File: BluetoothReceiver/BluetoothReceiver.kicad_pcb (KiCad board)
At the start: 4 copper layers, 48.4 x 40 mm, 54 parts, among them J1 EXT_ANTENNA, J2 SWD, J3 SPKR/HP, J4 MIC, J5 I2S, J6 I2C/UART, J7 USB, J8 3.3V, U1 STM32F413CHUx

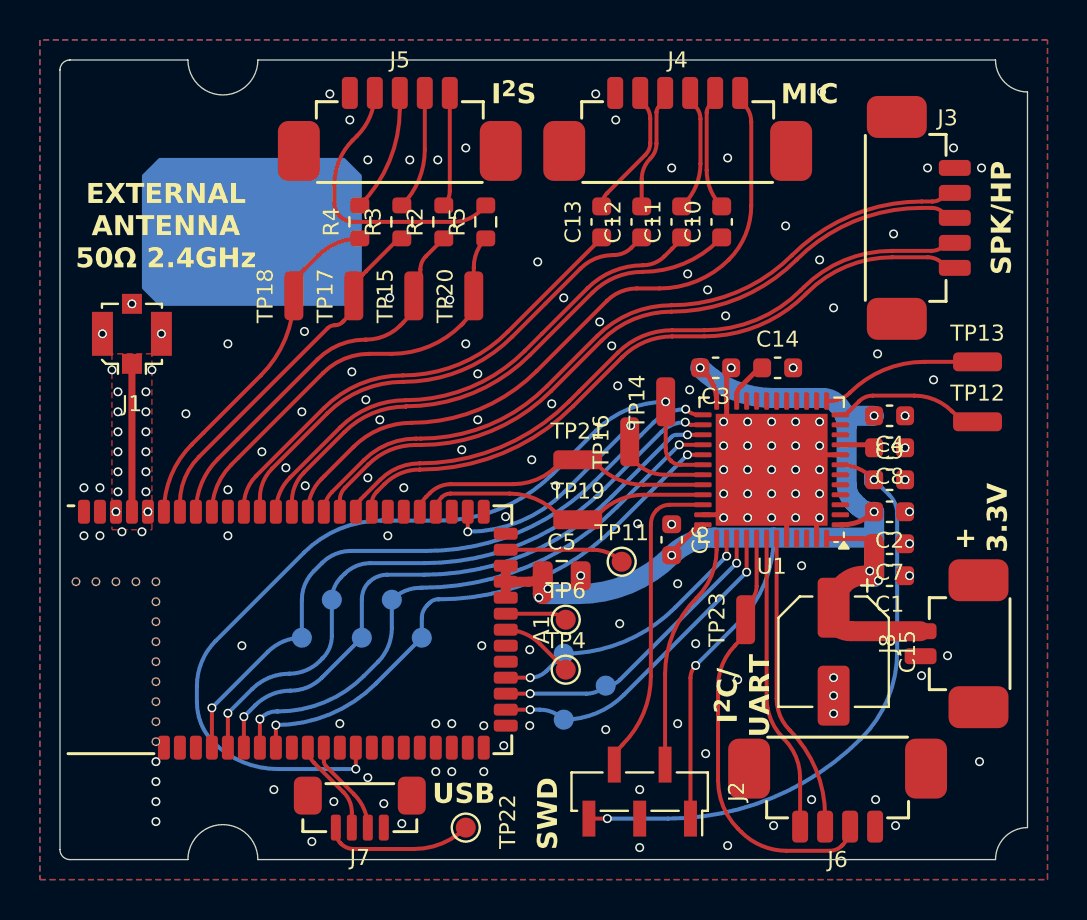
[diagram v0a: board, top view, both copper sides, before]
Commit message: BluetoothReceiver design done
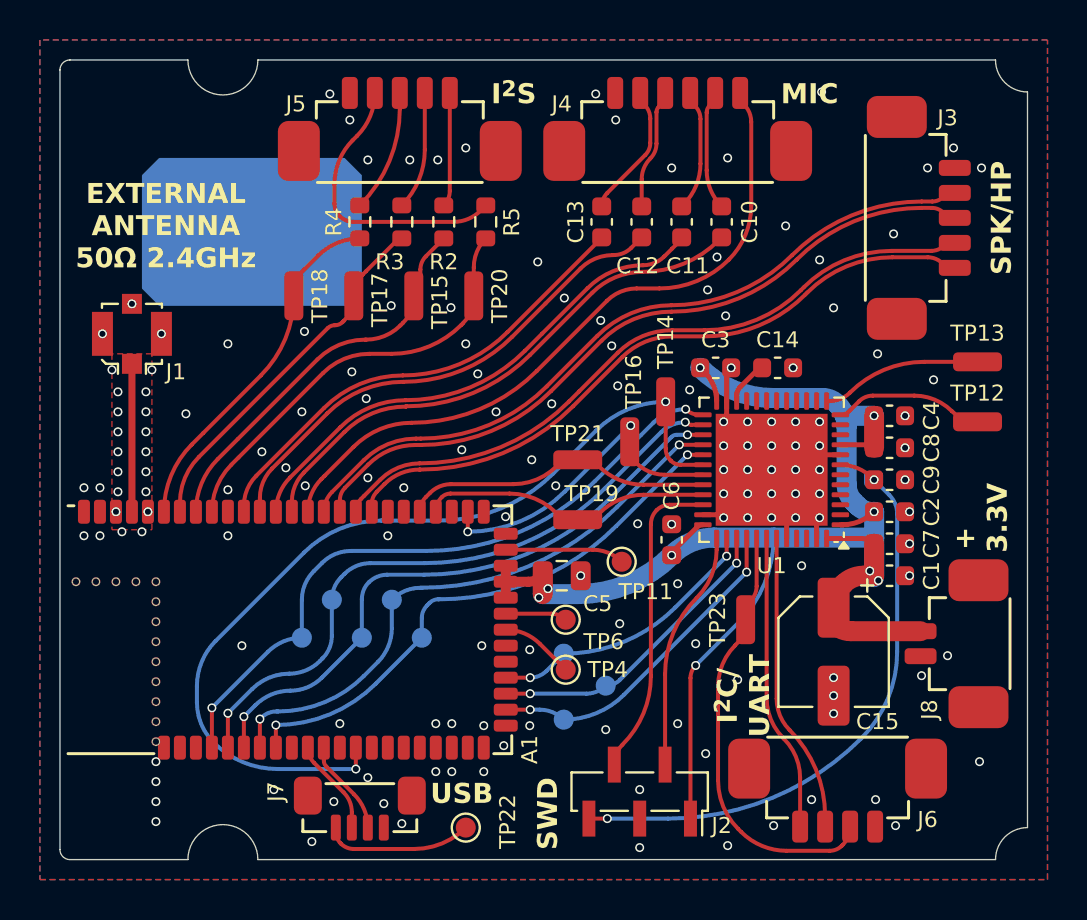
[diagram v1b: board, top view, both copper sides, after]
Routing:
- net +3.3V: track 75.4 -> 77.0 mm
- net GND: vias 158 -> 157
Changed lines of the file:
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@@
 		(tags "resistor")
 		(property "Reference" "TP21"
-			(at 0 -1.43 0)
+			(at 0 -1.3 0)
 			(layer "F.SilkS")
 			(effects
@@
 		(tags "test point SMD pad")
 		(property "Reference" "TP4"
-			(at 0 -1.448 0)
+			(at 2.1 0 0)
 			(layer "F.SilkS")
 			(effects
@@
 		(tags "resistor")
 		(property "Reference" "TP17"
-			(at 0 -1.43 90)
+			(at -0.2 1.3 90)
 			(layer "F.SilkS")
 			(effects
@@
 		(tags "resistor")
 		(property "Reference" "TP15"
-			(at 0 -1.43 90)
+			(at -0.3 1.3 90)
 			(layer "F.SilkS")
 			(effects
@@
 		(tags "resistor")
 		(property "Reference" "R4"
-			(at 0 -1.43 90)
+			(at 0 -1.3 90)
 			(layer "F.SilkS")
 			(effects
@@
 		(tags "capacitor")
 		(property "Reference" "C9"
-			(at 0 -1.43 0)
+			(at 2.1 0 90)
 			(layer "F.SilkS")
 			(effects
@@
 		(tags "capacitor")
 		(property "Reference" "C7"
-			(at 0 -1.43 360)
+			(at -2.1 0 90)
 			(layer "F.SilkS")
 			(effects
@@
 		(tags "capacitor")
 		(property "Reference" "C4"
-			(at 0 -1.43 360)
+			(at -2.1 0 90)
 			(layer "F.SilkS")
 			(effects
@@
 		(tags "resistor")
 		(property "Reference" "TP16"
-			(at 0 -1.43 90)
+			(at 3 0.2 90)
 			(layer "F.SilkS")
 			(effects
@@
 		(tags "resistor")
 		(property "Reference" "TP14"
-			(at 0 -1.43 90)
+			(at 3 0 90)
 			(layer "F.SilkS")
 			(effects
@@
 		(tags "capacitor electrolytic")
 		(property "Reference" "C15"
-			(at 0 -3.7 90)
+			(at 3.5 -2.2 180)
 			(layer "F.SilkS")
 			(effects
@@
 		(at 152.5 84.1)
 		(property "Reference" "J4"
-			(at 0 -4.1 0)
+			(at -5.8 -1.9 0)
 			(layer "F.SilkS")
 			(effects
@@
 		(tags "capacitor")
 		(property "Reference" "C8"
-			(at 0 -1.43 360)
+			(at -2.1 0 90)
 			(layer "F.SilkS")
 			(effects
@@
 		(tags "resistor")
 		(property "Reference" "TP19"
-			(at 0 -1.43 0)
+			(at 0.7 -1.3 0)
 			(layer "F.SilkS")
 			(effects
@@
 		(at 136.6 117.4 180)
 		(property "Reference" "J7"
-			(at 0 -2.5 180)
+			(at 4.2 0.8 -90)
 			(layer "F.SilkS")
 			(effects
@@
 		(tags "capacitor")
 		(property "Reference" "C5"
-			(at 0 -1.68 360)
+			(at 1.8 1.4 0)
 			(layer "F.SilkS")
 			(effects
@@
 		(tags "resistor")
 		(property "Reference" "TP23"
-			(at 0 -1.43 90)
+			(at 0 -1.4 90)
 			(layer "F.SilkS")
 			(effects
@@
 		(tags "resistor")
 		(property "Reference" "R3"
-			(at 0 -1.43 90)
+			(at -2 -0.6 180)
 			(layer "F.SilkS")
 			(effects
@@
 		(tags "capacitor")
 		(property "Reference" "C2"
-			(at 0 -1.43 360)
+			(at -2.1 0 90)
 			(layer "F.SilkS")
 			(effects
@@
 		(at 167.1 109.2 90)
 		(property "Reference" "J8"
-			(at 0 -4.1 90)
+			(at -3.3 -2 90)
 			(layer "F.SilkS")
 			(effects
@@
 		(tags "Surface mounted socket strip SMD 1x05 1.27mm single row style2 pin1 right")
 		(property "Reference" "J2"
-			(at 0 -4.85 90)
+			(at 1.7 -4.1 180)
 			(layer "F.SilkS")
 			(effects
@@
 		(tags "capacitor")
 		(property "Reference" "C10"
-			(at 0 -1.43 90)
+			(at 0 1.4 90)
 			(layer "F.SilkS")
 			(effects
@@
 		(tags "test point SMD pad")
 		(property "Reference" "TP11"
-			(at 0 -1.448 0)
+			(at 1.2 1.5 0)
 			(layer "F.SilkS")
 			(effects
@@
 		(tags "test point SMD pad")
 		(property "Reference" "TP6"
-			(at 0 -1.448 0)
+			(at 1.9 1.1 0)
 			(layer "F.SilkS")
 			(effects
@@
 		(tags "capacitor")
 		(property "Reference" "C14"
-			(at 0 -1.43 360)
+			(at 0 -1.4 360)
 			(layer "F.SilkS")
 			(effects
@@
 		(at 132.8 108.5 90)
 		(property "Reference" "A1"
-			(at 0 12.9 90)
+			(at -6 12.3 90)
 			(unlocked yes)
 			(layer "F.SilkS")
@@
 		(tags "resistor")
 		(property "Reference" "TP18"
-			(at 0 -1.43 90)
+			(at 0 1.3 90)
 			(layer "F.SilkS")
 			(effects
@@
 		(tags "resistor")
 		(property "Reference" "R2"
-			(at 0 -1.43 90)
+			(at -2 0 180)
 			(layer "F.SilkS")
 			(effects
@@
 		(tags "resistor")
 		(property "Reference" "R5"
-			(at 0 -1.43 90)
+			(at 0 1.3 90)
 			(layer "F.SilkS")
 			(effects
@@
 		(tags "mcrf hirose ufl u.fl microcoaxial")
 		(property "Reference" "J1"
-			(at 0 3.5 360)
+			(at 2.2 1.9 360)
 			(layer "F.SilkS")
 			(effects
@@
 		(tags "capacitor")
 		(property "Reference" "C3"
-			(at 0 -1.43 360)
+			(at 0 1.4 360)
 			(layer "F.SilkS")
 			(effects
@@
 		(at 138.6 84.1)
 		(property "Reference" "J5"
-			(at 0 -4.1 360)
+			(at -5.2 -1.9 360)
 			(layer "F.SilkS")
 			(effects
@@
 		(tags "capacitor")
 		(property "Reference" "C13"
-			(at 0 -1.43 90)
+			(at 0 -1.3 90)
 			(layer "F.SilkS")
 			(effects
@@
 		(tags "capacitor")
 		(property "Reference" "C12"
-			(at 0 -1.43 90)
+			(at -2.2 -0.2 180)
 			(layer "F.SilkS")
 			(effects
@@
 		(tags "QFN NoLead")
 		(property "Reference" "U1"
-			(at 0 -4.83 360)
+			(at 0 -4.8 360)
 			(layer "F.SilkS")
 			(effects
@@
 		(tags "capacitor")
 		(property "Reference" "C11"
-			(at 0 -1.43 90)
+			(at -2.2 0.3 180)
 			(layer "F.SilkS")
 			(effects
@@
 		(at 160.5 115.9 180)
 		(property "Reference" "J6"
-			(at 0 -4.1 360)
+			(at -4.5 -2.1 360)
 			(layer "F.SilkS")
 			(effects
@@
 		(tags "capacitor")
 		(property "Reference" "C6"
-			(at 0 -1.43 90)
+			(at -2.2 0 -90)
 			(layer "F.SilkS")
 			(effects
@@
 		(tags "capacitor")
 		(property "Reference" "C1"
-			(at 0 -1.43 360)
+			(at -2.1 0 90)
 			(layer "F.SilkS")
 			(effects
@@
 		(tags "resistor")
 		(property "Reference" "TP20"
-			(at 0 -1.43 90)
+			(at 0 1.3 90)
 			(layer "F.SilkS")
 			(effects
@@
 	)
 	(gr_text "USB"
-		(at 141.8 116.7 0)
+		(at 141.7 116.7 0)
 		(layer "F.SilkS" knockout)
 		(effects
@@
 	)
 	(via
-		(at 136.9 97)
+		(at 136.92 96.94)
 		(size 0.45)
 		(drill 0.3)
@@
 	)
 	(via
-		(at 141.1 92)
+		(at 141.16 92.39)
 		(size 0.45)
 		(drill 0.3)
@@
 	)
 	(via
-		(at 148.6 93.1)
+		(at 148.65 93.03)
 		(size 0.45)
 		(drill 0.3)
@@
 	)
 	(via
-		(at 142.5 98)
+		(at 143.415419 97.601286)
 		(size 0.45)
 		(drill 0.3)
@@
 	)
 	(via
-		(at 138.1 91.9)
+		(at 138.17 92.29)
 		(size 0.45)
 		(drill 0.3)
@@
 	)
 	(via
-		(at 146.8 91.9)
+		(at 146.83 91.91)
 		(size 0.45)
 		(drill 0.3)
@@
 	)
 	(via
-		(at 137.6 98)
-		(size 0.45)
-		(drill 0.3)
-		(layers "F.Cu" "B.Cu")
-		(free yes)
-		(net 2)
-	)
-	(via
 		(at 157.2 100.5)
 		(size 0.45)
@@
 	)
 	(via
-		(at 153 90.7)
+		(at 154.47 89.86)
 		(size 0.45)
 		(drill 0.3)
@@
 		(layer "F.Cu")
 		(net 5)
+	)
+	(segment
+		(start 162.325 97.8)
+		(end 162.325 99.4)
+		(width 1)
+		(layer "F.Cu")
+		(net 5)
